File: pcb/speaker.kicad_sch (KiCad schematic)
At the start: 6 parts, among them U2 LM386

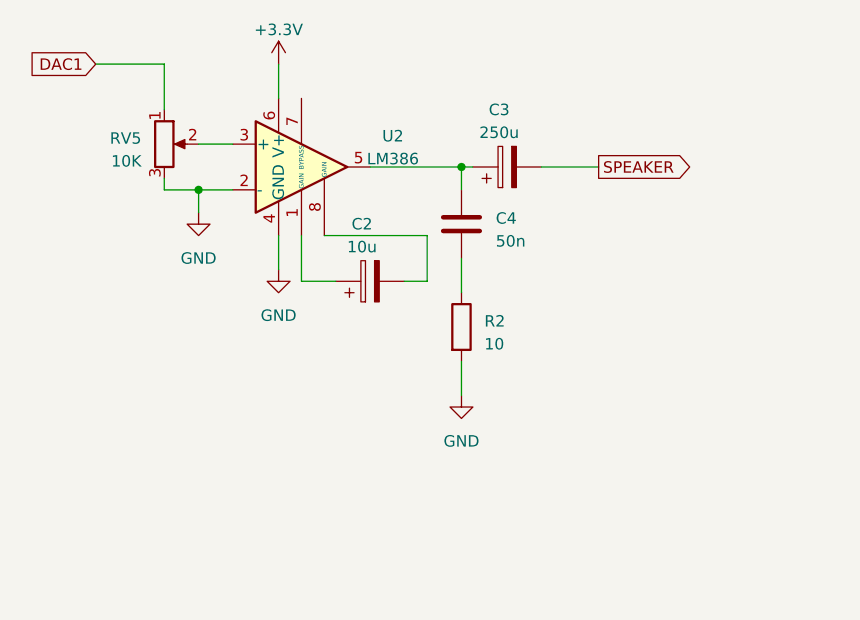
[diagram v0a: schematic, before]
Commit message: added some componentes to schematics and pcb
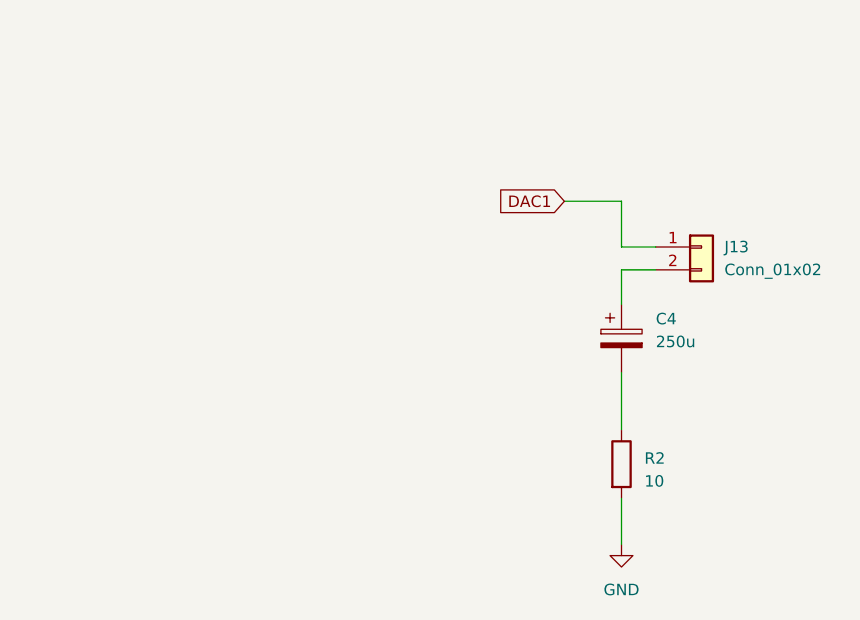
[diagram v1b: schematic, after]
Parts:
- removed C2: 10u, Capacitor_SMD:CP_Elec_5x3, symbol Device:C_Polarized
- removed C4: 50n, Capacitor_SMD:C_0805_2012Metric_Pad1.18x1.45mm_HandSolder, symbol Device:C
- removed RV5: 10K, Potentiometer_SMD:Potentiometer_Bourns_3314G_Vertical, symbol Device:R_Potentiometer
- removed U2: LM386, symbol Amplifier_Audio:LM386
- added J13: Conn_01x02, Connector_PinHeader_2.54mm:PinHeader_1x02_P2.54mm_Vertical, symbol Connector_Generic:Conn_01x02
- renumbered C3 to C4
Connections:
- net SPEAKER is gone; now on an unnamed net: C4.2
- net DAC1: now also J13.1 (Pin_1)
- net at C4.1: now also J13.2 (Pin_2)
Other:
- title: (none) -> vbass
- moved on the sheet: C4, R2
